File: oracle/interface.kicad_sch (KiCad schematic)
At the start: 54 parts, among them J1 I2C multiplexer, J2 LCD RGB LED, J3 USB-C U-N, J4 USB-C U-S, J5 Banana connector pads, SW1 12mmx12mm, SW10 12mmx12mm, SW11 12mmx12mm, SW12 12mmx12mm, SW13 12mmx12mm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

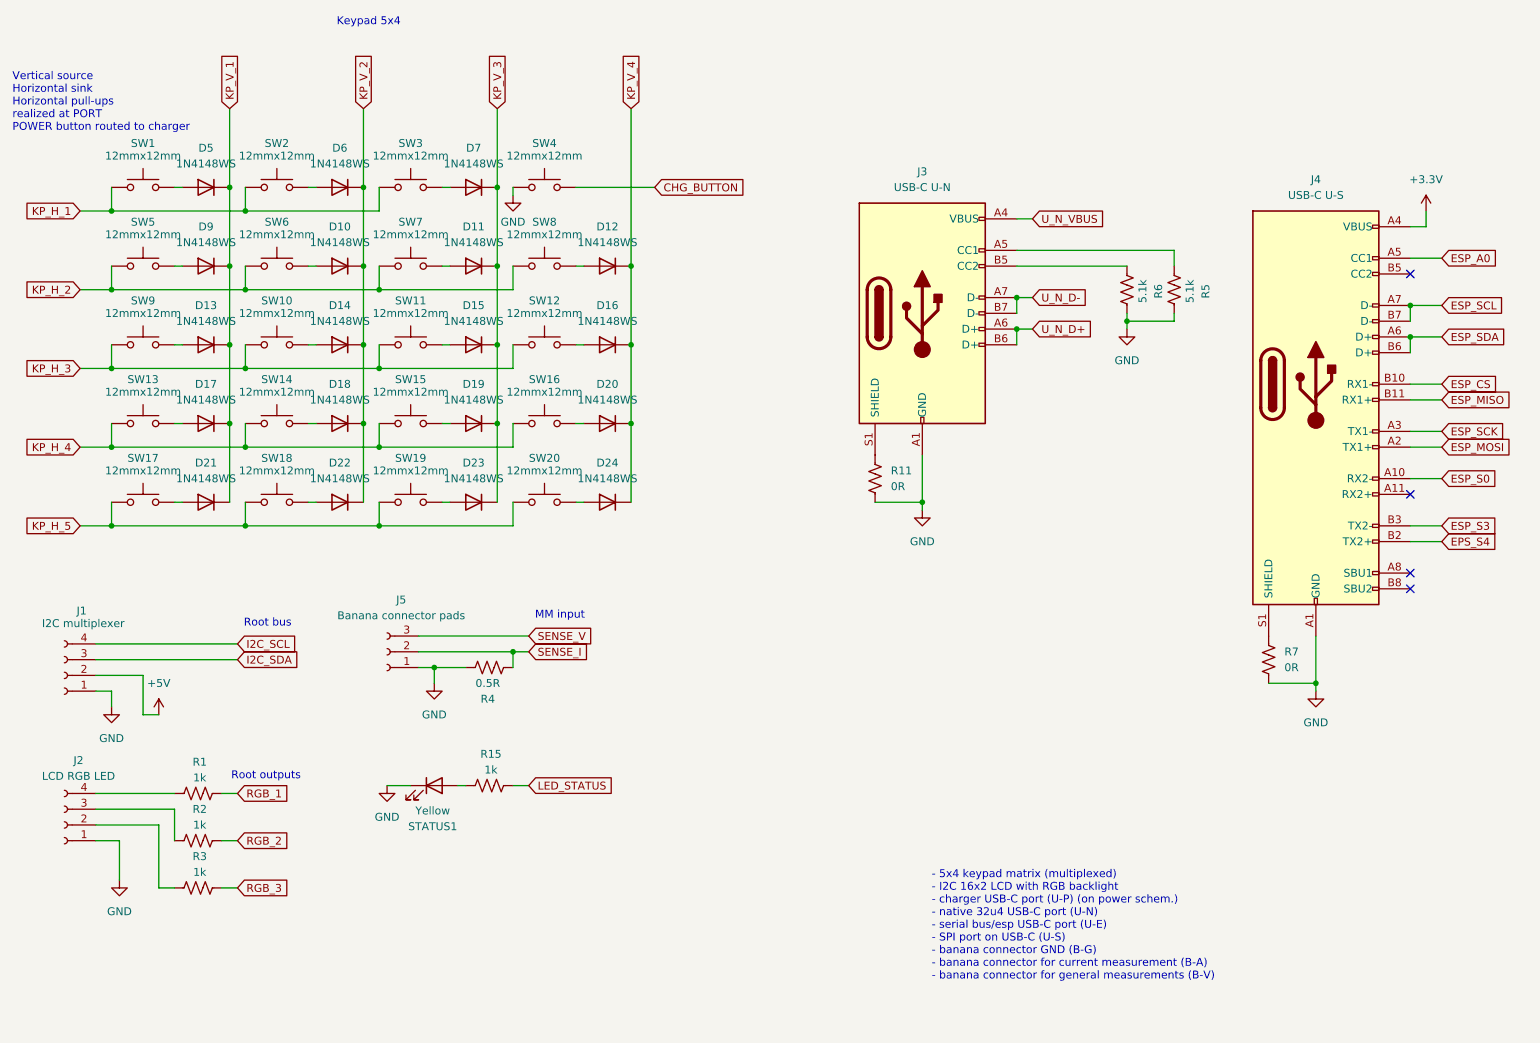
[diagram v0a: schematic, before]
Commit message: add n_core firmware add e_core firmware stub update PCB
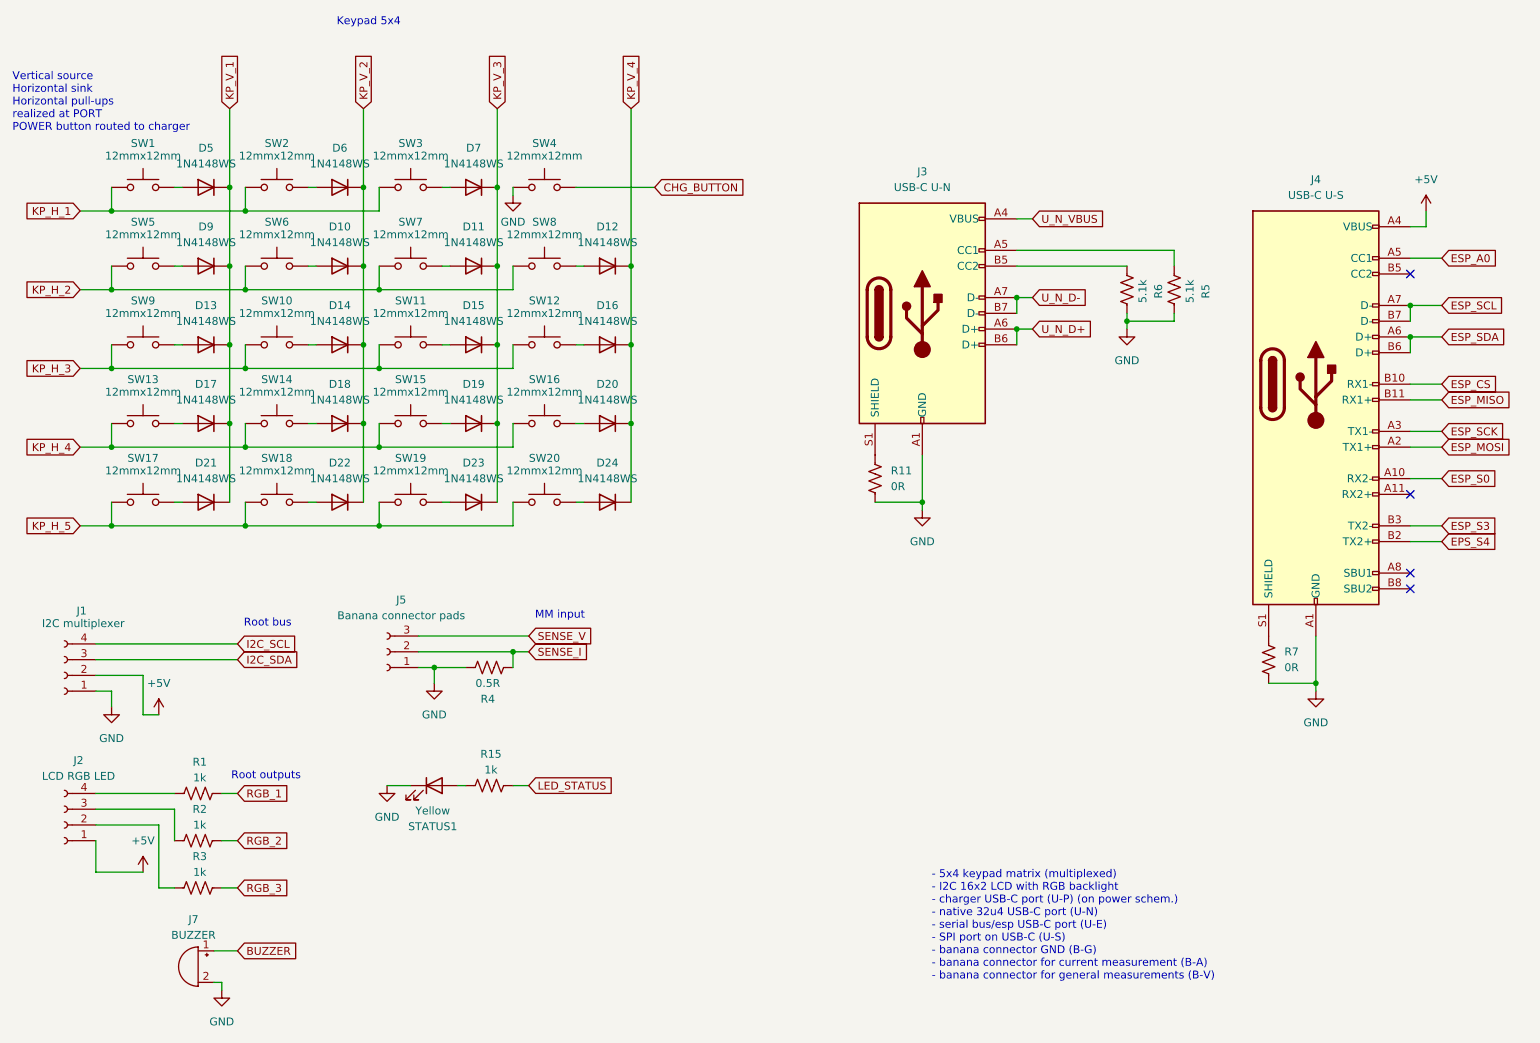
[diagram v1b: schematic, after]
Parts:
- added J7: BUZZER, Connector_PinHeader_2.54mm:PinHeader_1x02_P2.54mm_Vertical, symbol Device:Buzzer
- J4: footprint Connector_USB:USB_C_Receptacle_Amphenol_12401610E4-2A -> Connector_USB:USB_C_Receptacle_Amphenol_12401548E4-2A
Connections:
- net +3.3V is gone; now on net +5V: J4.A4 (VBUS), J4.A9 (VBUS), J4.B4 (VBUS), J4.B9 (VBUS)
- net +5V: now also J2.1 (Pin_1)
- net GND: now also J7.2 (-); no longer J2.1 (Pin_1)
- new net BUZZER: J7.1 (+)
